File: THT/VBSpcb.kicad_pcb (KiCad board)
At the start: 2 copper layers, 37.8 x 40 mm, 15 parts, among them J1 Video In GND, J2 DB25_Receptacle, J3 Video In Sig, U1 LF356

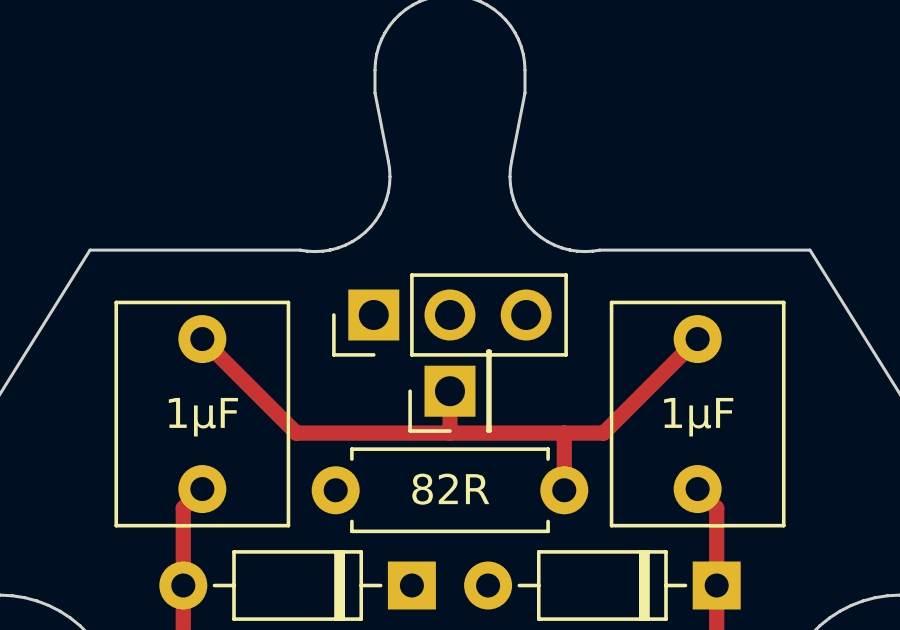
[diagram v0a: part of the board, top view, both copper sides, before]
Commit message: Added SMT version and moved THT to it's own folder
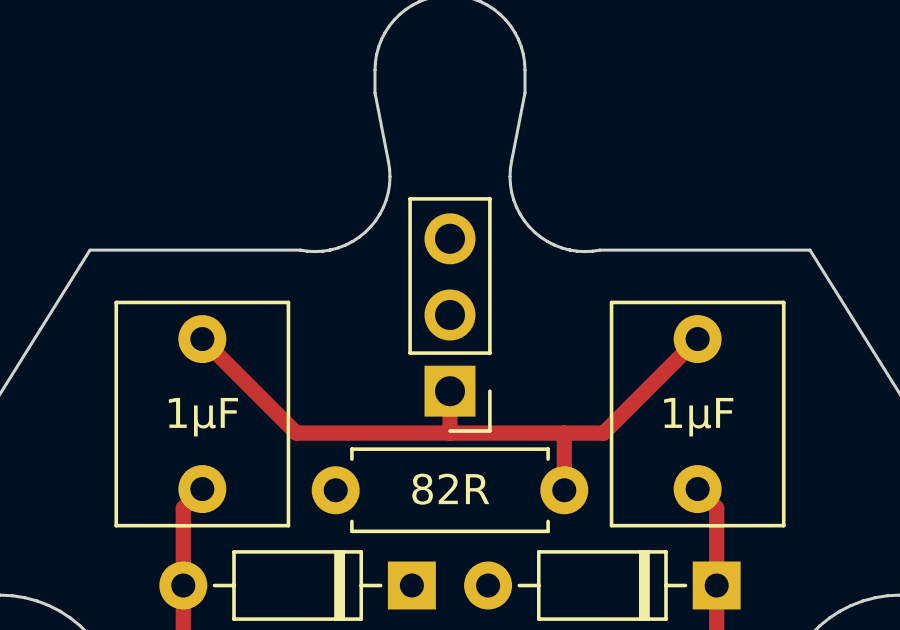
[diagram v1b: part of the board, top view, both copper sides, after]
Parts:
- removed J3: Video In Sig, Connector_PinHeader_2.54mm:PinHeader_1x01_P2.54mm_Vertical
- moved J1 3.59 mm to (116.8, 67.8), turned to 180 degrees
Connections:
- C1 pad 1: Net-(J3-Pin_1) -> Net-(J1-Pin_1)
- C2 pad 1: Net-(J3-Pin_1) -> Net-(J1-Pin_1)
- J1 pad 1: GND -> Net-(J1-Pin_1)
- R1 pad 1: Net-(J3-Pin_1) -> Net-(J1-Pin_1)
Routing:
- net Net-(J3-Pin_1): track 22.4 -> 0.00 mm
- net Net-(J1-Pin_1): track 0.00 -> 22.4 mm
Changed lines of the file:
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@@
   (net 31 "unconnected-(U1-NULL-Pad5)")
   (net 32 "unconnected-(U1-NC-Pad8)")
-  (net 33 "Net-(J3-Pin_1)")
+  (net 33 "Net-(J1-Pin_1)")
   (footprint "Capacitor_THT:C_Rect_L7.2mm_W5.5mm_P5.00mm_FKS2_FKP2_MKS2_MKP2" (layer "F.Cu")
     (at 125.095 66.08 -90)
@@
       (stroke (width 0.1) (type solid)) (layer "F.Fab"))
     (pad "1" thru_hole circle (at 0 0 270) (size 1.6 1.6) (drill 0.8) (layers "*.Cu" "*.Mask")
-      (net 33 "Net-(J3-Pin_1)") (pintype "passive"))
+      (net 33 "Net-(J1-Pin_1)") (pintype "passive"))
     (pad "2" thru_hole circle (at 5 0 270) (size 1.6 1.6) (drill 0.8) (layers "*.Cu" "*.Mask")
       (net 2 "Net-(D2-K)") (pintype "passive"))
@@
       (stroke (width 0.1) (type solid)) (layer "F.Fab"))
     (pad "1" thru_hole circle (at 0 0 270) (size 1.6 1.6) (drill 0.8) (layers "*.Cu" "*.Mask")
-      (net 33 "Net-(J3-Pin_1)") (pintype "passive"))
+      (net 33 "Net-(J1-Pin_1)") (pintype "passive"))
     (pad "2" thru_hole circle (at 5 0 270) (size 1.6 1.6) (drill 0.8) (layers "*.Cu" "*.Mask")
       (net 1 "Net-(D1-A)") (pintype "passive"))
     (model "${KICAD6_3DMODEL_DIR}/Capacitor_THT.3dshapes/C_Rect_L7.2mm_W5.5mm_P5.00mm_FKS2_FKP2_MKS2_MKP2.wrl"
-      (offset (xyz 0 0 0))
-      (scale (xyz 1 1 1))
-      (rotate (xyz 0 0 0))
-    )
-  )
-  (footprint "Connector_PinHeader_2.54mm:PinHeader_1x01_P2.54mm_Vertical" (layer "F.Cu")
-    (at 116.84 67.818 90)
-    (descr "Through hole straight pin header, 1x01, 2.54mm pitch, single row")
-    (tags "Through hole pin header THT 1x01 2.54mm single row")
-    (property "Sheetfile" "VBSpcb.kicad_sch")
-    (property "Sheetname" "")
-    (property "ki_description" "Generic connector, single row, 01x01, script generated (kicad-library-utils/schlib/autogen/connector/)")
-    (property "ki_keywords" "connector")
-    (attr through_hole)
-    (fp_text reference "J3" (at 0 -2.33 90) (layer "F.SilkS") hide
-        (effects (font (size 1 1) (thickness 0.15)))
-    )
-    (fp_text value "Video In Sig" (at 0 2.33 90) (layer "F.Fab") hide
-        (effects (font (size 1 1) (thickness 0.15)))
-    )
-    (fp_text user "${REFERENCE}" (at 0 0) (layer "F.Fab") hide
-        (effects (font (size 1 1) (thickness 0.15)))
-    )
-    (fp_line (start -1.33 -1.33) (end 0 -1.33)
-      (stroke (width 0.12) (type solid)) (layer "F.SilkS"))
-    (fp_line (start -1.33 0) (end -1.33 -1.33)
-      (stroke (width 0.12) (type solid)) (layer "F.SilkS"))
-    (fp_line (start -1.33 1.27) (end -1.33 1.33)
-      (stroke (width 0.12) (type solid)) (layer "F.SilkS"))
-    (fp_line (start -1.33 1.27) (end 1.33 1.27)
-      (stroke (width 0.12) (type solid)) (layer "F.SilkS"))
-    (fp_line (start -1.33 1.33) (end 1.33 1.33)
-      (stroke (width 0.12) (type solid)) (layer "F.SilkS"))
-    (fp_line (start 1.33 1.27) (end 1.33 1.33)
-      (stroke (width 0.12) (type solid)) (layer "F.SilkS"))
-    (fp_line (start -1.8 -1.8) (end -1.8 1.8)
-      (stroke (width 0.05) (type solid)) (layer "F.CrtYd"))
-    (fp_line (start -1.8 1.8) (end 1.8 1.8)
-      (stroke (width 0.05) (type solid)) (layer "F.CrtYd"))
-    (fp_line (start 1.8 -1.8) (end -1.8 -1.8)
-      (stroke (width 0.05) (type solid)) (layer "F.CrtYd"))
-    (fp_line (start 1.8 1.8) (end 1.8 -1.8)
-      (stroke (width 0.05) (type solid)) (layer "F.CrtYd"))
-    (fp_line (start -1.27 -0.635) (end -0.635 -1.27)
-      (stroke (width 0.1) (type solid)) (layer "F.Fab"))
-    (fp_line (start -1.27 1.27) (end -1.27 -0.635)
-      (stroke (width 0.1) (type solid)) (layer "F.Fab"))
-    (fp_line (start -0.635 -1.27) (end 1.27 -1.27)
-      (stroke (width 0.1) (type solid)) (layer "F.Fab"))
-    (fp_line (start 1.27 -1.27) (end 1.27 1.27)
-      (stroke (width 0.1) (type solid)) (layer "F.Fab"))
-    (fp_line (start 1.27 1.27) (end -1.27 1.27)
-      (stroke (width 0.1) (type solid)) (layer "F.Fab"))
-    (pad "1" thru_hole rect (at 0 0 90) (size 1.7 1.7) (drill 1) (layers "*.Cu" "*.Mask")
-      (net 33 "Net-(J3-Pin_1)") (pinfunction "Pin_1") (pintype "passive"))
-    (model "${KICAD6_3DMODEL_DIR}/Connector_PinHeader_2.54mm.3dshapes/PinHeader_1x01_P2.54mm_Vertical.wrl"
       (offset (xyz 0 0 0))
       (scale (xyz 1 1 1))
@@
       (stroke (width 0.1) (type solid)) (layer "F.Fab"))
     (pad "1" thru_hole circle (at 0 0 180) (size 1.6 1.6) (drill 0.8) (layers "*.Cu" "*.Mask")
-      (net 33 "Net-(J3-Pin_1)") (pintype "passive"))
+      (net 33 "Net-(J1-Pin_1)") (pintype "passive"))
     (pad "2" thru_hole oval (at 7.62 0 180) (size 1.6 1.6) (drill 0.8) (layers "*.Cu" "*.Mask")
       (net 4 "GND") (pintype "passive"))
@@
   )
   (footprint "Connector_PinHeader_2.54mm:PinHeader_1x03_P2.54mm_Vertical" (layer "F.Cu")
-    (at 114.3 65.278 90)
+    (at 116.84 67.818 180)
     (descr "Through hole straight pin header, 1x03, 2.54mm pitch, single row")
     (tags "Through hole pin header THT 1x03 2.54mm single row")
@@
     (property "ki_keywords" "connector")
     (attr through_hole)
-    (fp_text reference "J1" (at 0 -2.33 90) (layer "F.SilkS") hide
-        (effects (font (size 1 1) (thickness 0.15)))
-    )
-    (fp_text value "Video In GND" (at 0 7.41 90) (layer "F.SilkS") hide
-        (effects (font (size 1 1) (thickness 0.15)))
-    )
-    (fp_text user "${REFERENCE}" (at 0 2.54) (layer "F.Fab") hide
+    (fp_text reference "J1" (at 0 -2.33) (layer "F.SilkS") hide
+        (effects (font (size 1 1) (thickness 0.15)))
+    )
+    (fp_text value "Video In GND" (at 0 7.41) (layer "F.SilkS") hide
+        (effects (font (size 1 1) (thickness 0.15)))
+    )
+    (fp_text user "${REFERENCE}" (at 0 2.54 90) (layer "F.Fab") hide
         (effects (font (size 1 1) (thickness 0.15)))
     )
@@
     (fp_line (start 1.27 6.35) (end -1.27 6.35)
       (stroke (width 0.1) (type solid)) (layer "F.Fab"))
-    (pad "1" thru_hole rect (at 0 0 90) (size 1.7 1.7) (drill 1) (layers "*.Cu" "*.Mask")
-      (net 4 "GND") (pinfunction "Pin_1") (pintype "passive"))
-    (pad "2" thru_hole oval (at 0 2.54 90) (size 1.7 1.7) (drill 1) (layers "*.Cu" "*.Mask")
+    (pad "1" thru_hole rect (at 0 0 180) (size 1.7 1.7) (drill 1) (layers "*.Cu" "*.Mask")
+      (net 33 "Net-(J1-Pin_1)") (pinfunction "Pin_1") (pintype "passive"))
+    (pad "2" thru_hole oval (at 0 2.54 180) (size 1.7 1.7) (drill 1) (layers "*.Cu" "*.Mask")
       (net 4 "GND") (pinfunction "Pin_2") (pintype "passive"))
-    (pad "3" thru_hole oval (at 0 5.08 90) (size 1.7 1.7) (drill 1) (layers "*.Cu" "*.Mask")
+    (pad "3" thru_hole oval (at 0 5.08 180) (size 1.7 1.7) (drill 1) (layers "*.Cu" "*.Mask")
       (net 4 "GND") (pinfunction "Pin_3") (pintype "passive"))
     (model "${KICAD6_3DMODEL_DIR}/Connector_PinHeader_2.54mm.3dshapes/PinHeader_1x03_P2.54mm_Vertical.wrl"
